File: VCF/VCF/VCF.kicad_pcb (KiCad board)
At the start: 4 copper layers, 98 x 80 mm, 91 parts, among them J1 Conn_02x05_Odd_Even, J2 Conn_01x08, J3 Conn_01x08, Q1 2N3904, Q2 2N3904, Q3 2N3906, Q4 2N3906, U1 TL072, U2 TL074, U3 LM13700, U4 TL072, U5 TL072, U6 LM13700

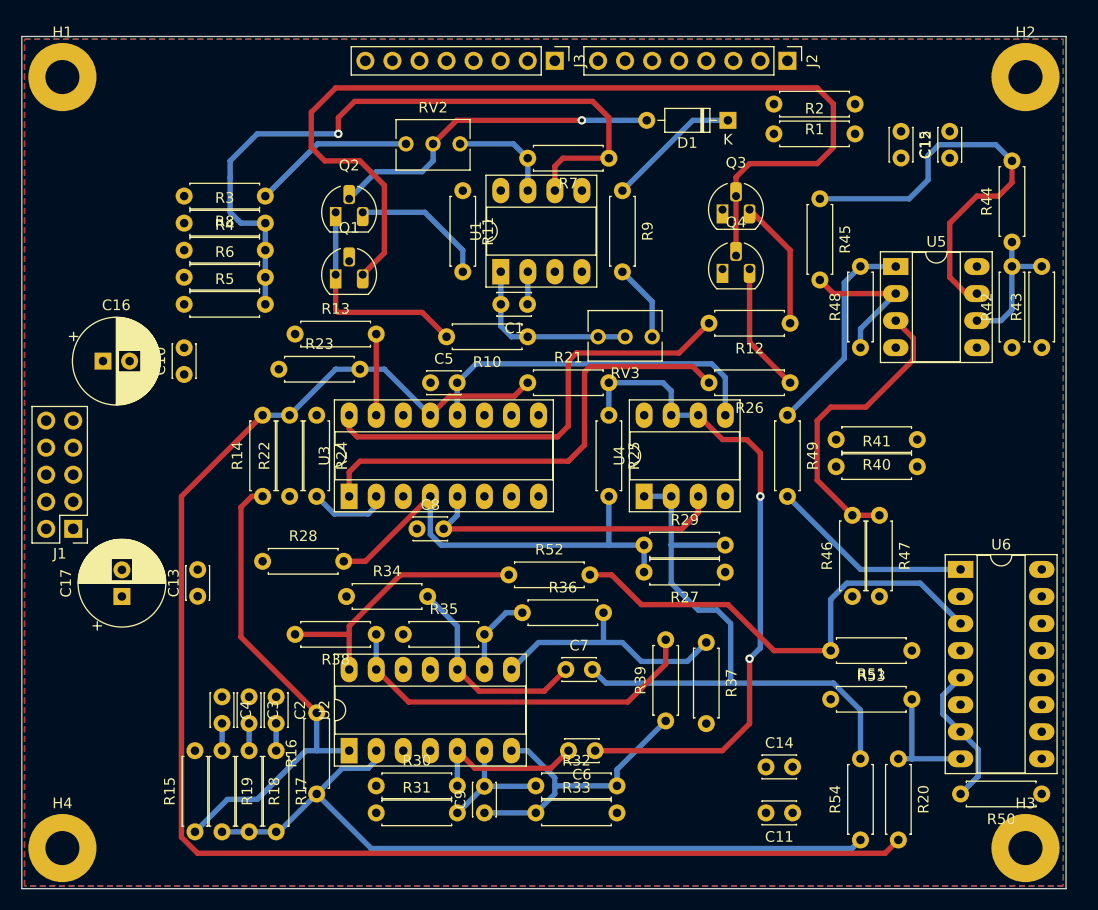
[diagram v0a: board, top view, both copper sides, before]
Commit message: VCF - fully routed
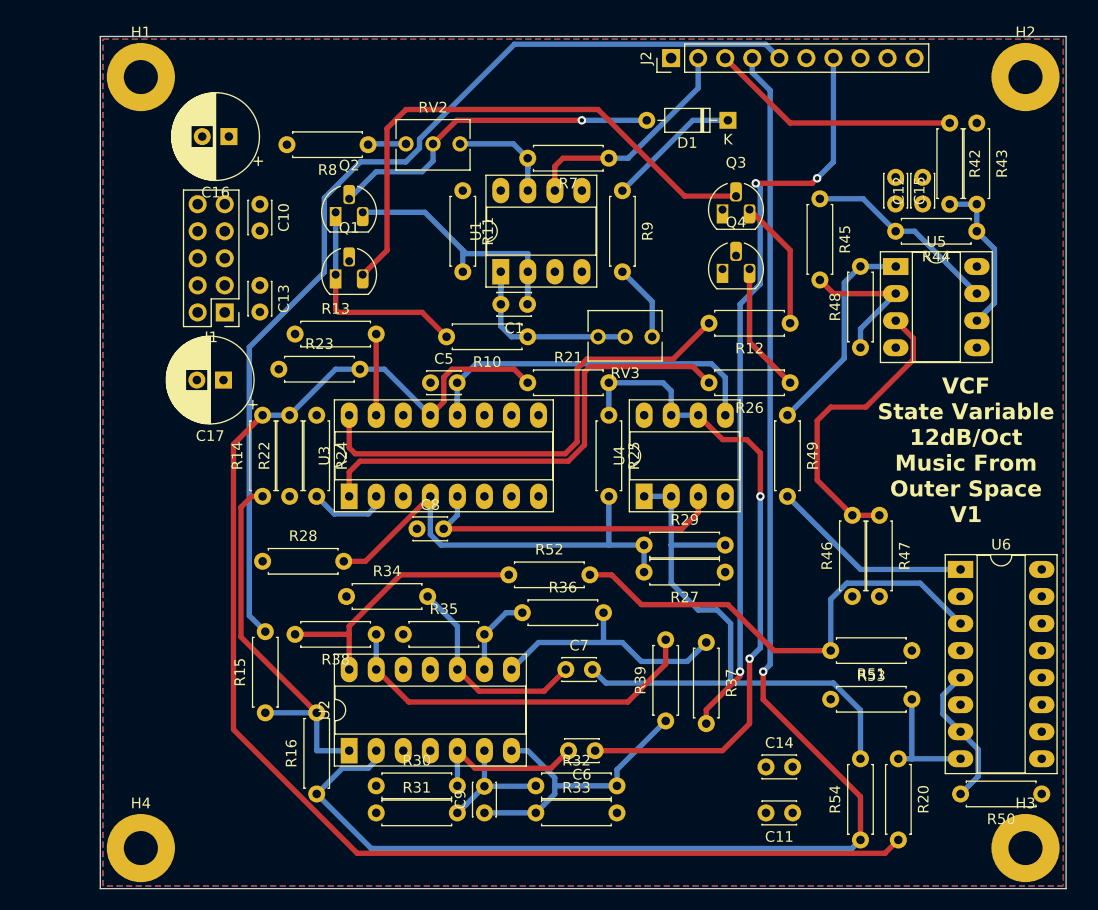
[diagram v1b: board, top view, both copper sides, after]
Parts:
- removed C2, C3, C4: 100nF, Capacitor_THT:C_Disc_D3.0mm_W2.0mm_P2.50mm
- removed J3: Conn_01x08, Connector_PinHeader_2.54mm:PinHeader_1x08_P2.54mm_Vertical
- removed R1, R2: 33K, Library:R_Axial_DIN0207_L6.3mm_D2.5mm_P7.62mm_Horizontal
- removed R17, R18, R19: 1M, Library:R_Axial_DIN0207_L6.3mm_D2.5mm_P7.62mm_Horizontal
- removed R3, R4, R5, R6: 100K, Library:R_Axial_DIN0207_L6.3mm_D2.5mm_P7.62mm_Horizontal
- removed R40, R41: 49.9K, Library:R_Axial_DIN0207_L6.3mm_D2.5mm_P7.62mm_Horizontal
- J2: value Conn_01x08 -> Conn_01x10; footprint Connector_PinHeader_2.54mm:PinHeader_1x08_P2.54mm_Vertical -> Connector_PinHeader_2.54mm:PinHeader_1x10_P2.54mm_Vertical
- moved C13 29.8 mm to (70.1, 48.0), turned to -90 degrees
- moved J1 24.8 mm to (66.8, 50.5)
- moved C16 24.2 mm to (67.2, 34.0), turned to 180 degrees
- moved C17 22.4 mm to (66.7, 56.9), turned to 180 degrees
- moved R43 21.9 mm to (137.4, 32.8), turned to -90 degrees
- moved R42 21.9 mm to (134.9, 32.8), turned to -90 degrees
- moved C10 17.5 mm to (70.1, 40.4), turned to -90 degrees
- moved R15 13.0 mm to (70.6, 88.1)
- moved J2 10.9 mm to (108.7, 26.7), turned to 90 degrees
- moved R8 10.8 mm to (80.3, 34.8)
- moved H1 7.37 mm to (58.9, 28.4)
- moved H4 7.37 mm to (58.9, 100.8)
- moved C12 5.01 mm to (132.3, 40.4)
- moved C15 4.35 mm to (129.8, 37.9)
- moved R44 3.45 mm to (137.4, 42.9), turned to 180 degrees
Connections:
- J2 pad 1: CO3 -> RES
- J2 pad 2: CO2 -> CV/CO
- J2 pad 3: CO1 -> XRES
- J2 pad 4: RES3 -> AIN
- J2 pad 5: RES2 -> HP
- J2 pad 6: RES1 -> BP
- J2 pad 7: CV1 -> LP
- J2 pad 8: CV2 -> +12V
- R16 pad 1: Net-(U2A--) -> AIN
- R43 pad 1: RES2 -> RES
- R54 pad 1: Net-(U2A--) -> AIN
- R7 pad 1: Net-(U1B--) -> CV/CO
- U1 pad 6: Net-(U1B--) -> CV/CO
- U2 pad 2: Net-(U2A--) -> AIN
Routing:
- net AIN: track 0.00 -> 139.5 mm, vias 0 -> 1
- net HP: track 0.00 -> 94.0 mm
- net BP: track 0.00 -> 79.3 mm
- net Net-(U2A--): track 71.7 -> 0.00 mm
- net LP: track 0.00 -> 70.9 mm, vias 0 -> 3
- net Net-(U1B--): track 67.0 -> 0.00 mm, vias 1 -> 0
- net Net-(Q1-C): track 93.2 -> 51.5 mm
- net RES: track 0.00 -> 31.2 mm
- net XRES: track 0.00 -> 23.6 mm
- net CV/CO: track 0.00 -> 21.6 mm
- net Net-(R44-Pad2): track 39.8 -> 18.4 mm
- net Net-(R8-Pad1): track 15.2 -> 3.59 mm
- net Net-(U3A--): track 141.0 -> 130.5 mm
- net Net-(R14-Pad1): track 45.9 -> 36.1 mm
- net Net-(Q2-C): track 16.0 -> 25.4 mm
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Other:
- board size 98 x 80 mm -> 90.7 x 80 mm
- board text added: "VCF State Variable 12dB/Oct Music From Outer Space V1"

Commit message: minor
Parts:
- moved D1 5.29 mm to (111.0, 36.8), turned to 135 degrees
- moved H1 4.06 mm to (63.0, 28.4)
- moved H4 4.06 mm to (63.0, 100.8)
- moved J1 1.80 mm to (65.5, 51.8)
- moved C16 1.70 mm to (68.3, 35.3)
- moved C11 1.64 mm to (69.1, 49.3)
- moved C10 1.63 mm to (69.1, 41.7)
- moved C17 1.20 mm to (66.0, 57.9)
- moved C14 0.76 mm to (132.3, 39.6)
- moved C15 0.76 mm to (129.8, 37.1)
- moved C5 0.25 mm to (86.1, 56.9)
- moved R19 0.25 mm to (95.2, 56.9)
- renumbered C13 to C11, C11 to C12, C14 to C13, C12 to C14, C6 to C4, C9 to C6, C1 to C7, C7 to C8, C8 to C9, RV3 to HighFreqComp1, Q3 to Q1, Q4 to Q2, Q2 to Q3, Q1 to Q4, R15 to R11, R54 to R12, R14 to R13, R20 to R14, R13 to R15, R22 to R16, R7 to R17, R23 to R18, R21 to R19, R30 to R20, R12 to R21, R31 to R22, R8 to R23, R32 to R26, R33 to R28, R28 to R29, R9 to R30, R26 to R31, R29 to R32, R10 to R33, R11 to R34, R34 to R35, R35 to R36, R36 to R37, R39 to R38, R37 to R39, R38 to R40, R42 to R43, R43 to R44, R44 to R45, R45 to R46, R46 to R47, R47 to R49, R52 to R50, R53 to R51, R49 to R52, R50 to R53, R51 to R54, R16 to R6, U2 to U1, U1 to U2, RV2 to V/Oct1
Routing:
- net Net-(Q1-B): track 51.5 -> 57.1 mm
- net Net-(D1-K): track 12.6 -> 7.80 mm
- net HP: track 94.0 -> 95.5 mm
- net Net-(U4B-+): track 34.6 -> 33.2 mm
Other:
- board size 90.7 x 80 mm -> 86.6 x 80 mm
- board text added: "+12V"
- board text added: "-12V"
- board text added: "AIN"
- board text added: "BP"
- board text added: "CV"
- board text added: "GND"
- board text added: "HP"
- board text added: "LP"
- board text added: "RES"
- board text added: "XRES"

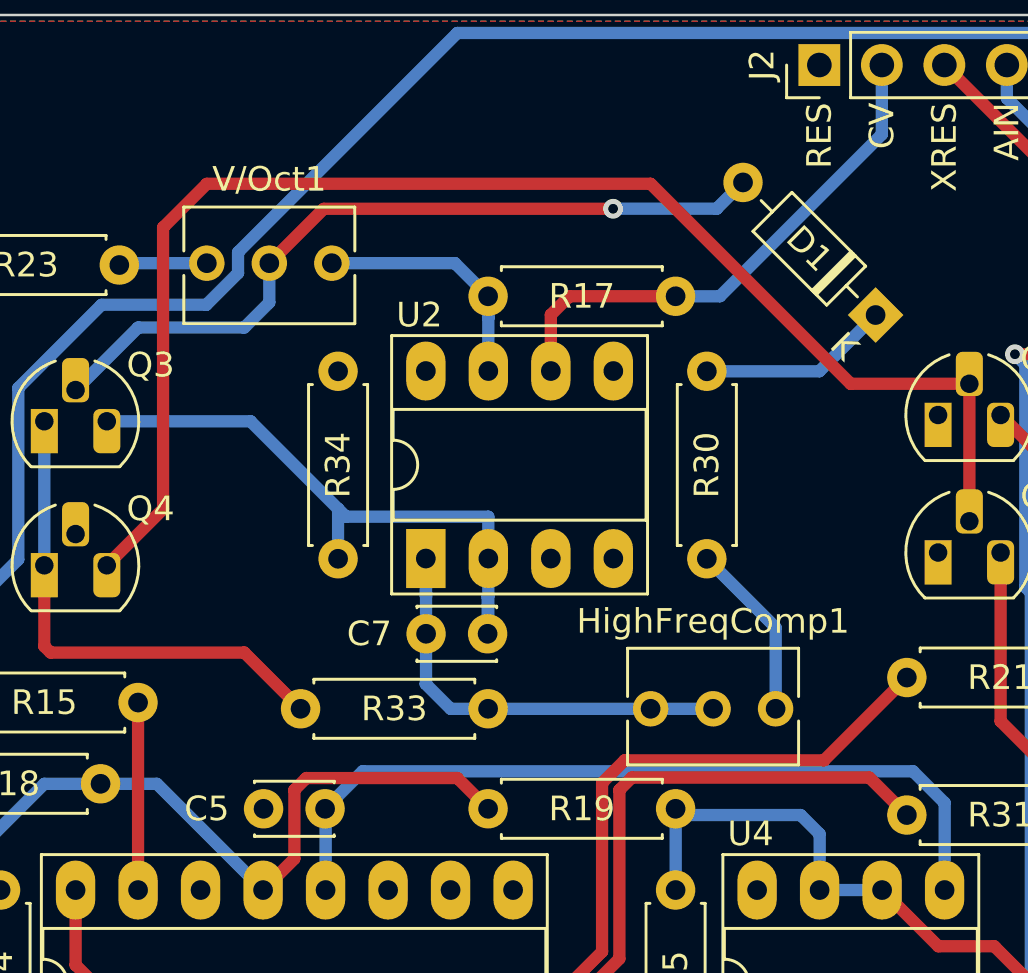
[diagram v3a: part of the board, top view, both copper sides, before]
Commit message: VCF - fix some components value
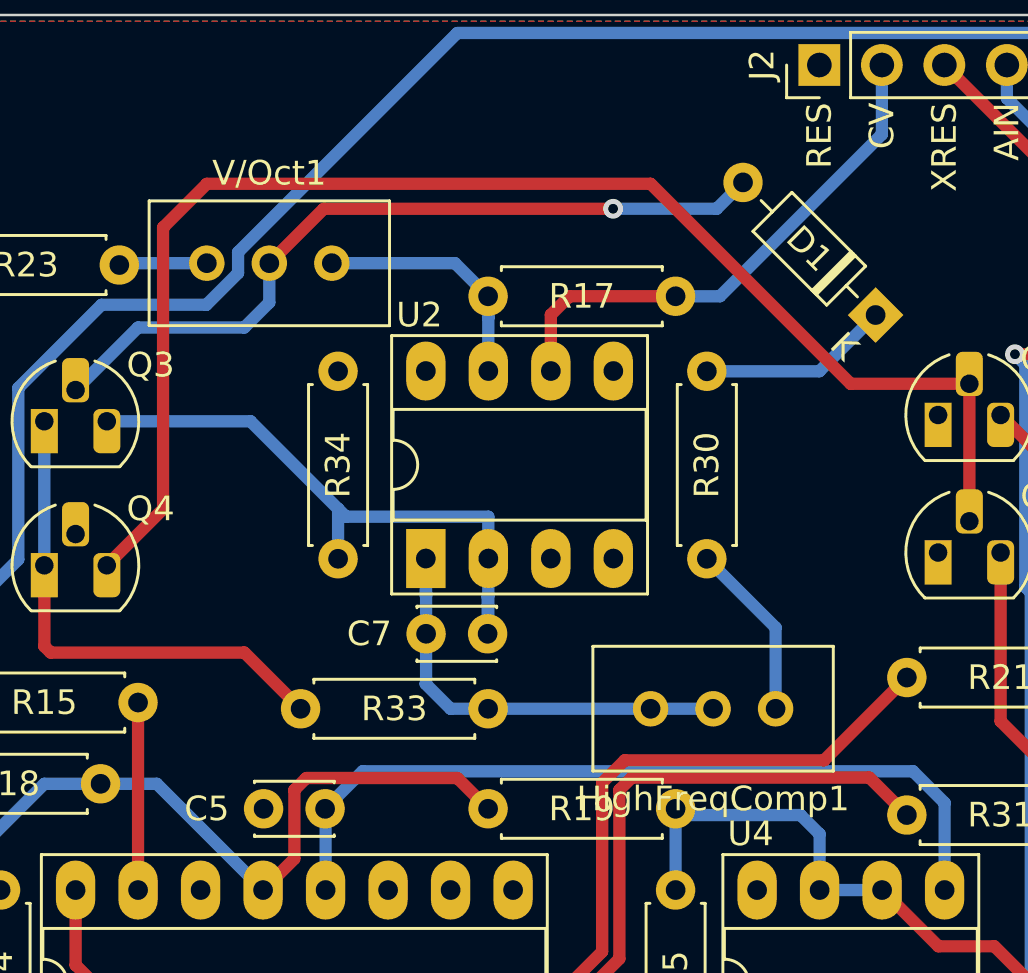
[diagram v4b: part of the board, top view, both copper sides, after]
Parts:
- HighFreqComp1: value 100R -> 2K; footprint Potentiometer_THT:Potentiometer_Bourns_3266Y_Vertical -> Potentiometer_THT:Potentiometer_Bourns_3296W_Vertical
- R17: value 100K -> 2K
- V/Oct1: footprint Potentiometer_THT:Potentiometer_Bourns_3266Y_Vertical -> Potentiometer_THT:Potentiometer_Bourns_3296W_Vertical
